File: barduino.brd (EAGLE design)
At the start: 54.9 x 47.4 mm, 25 parts, among them Q2 16MHz, X1 MINI-USB-PWR

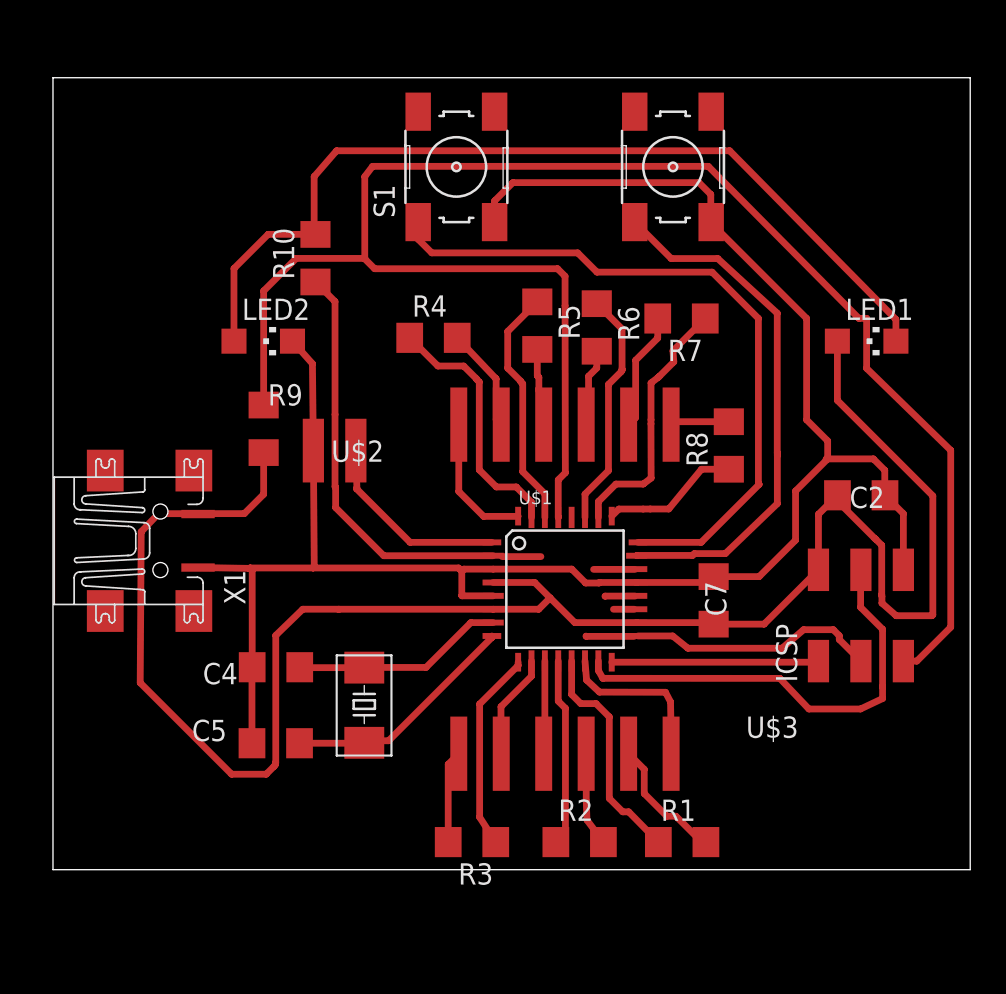
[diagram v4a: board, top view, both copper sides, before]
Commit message: update sch to correctly light AM/PM LEDs
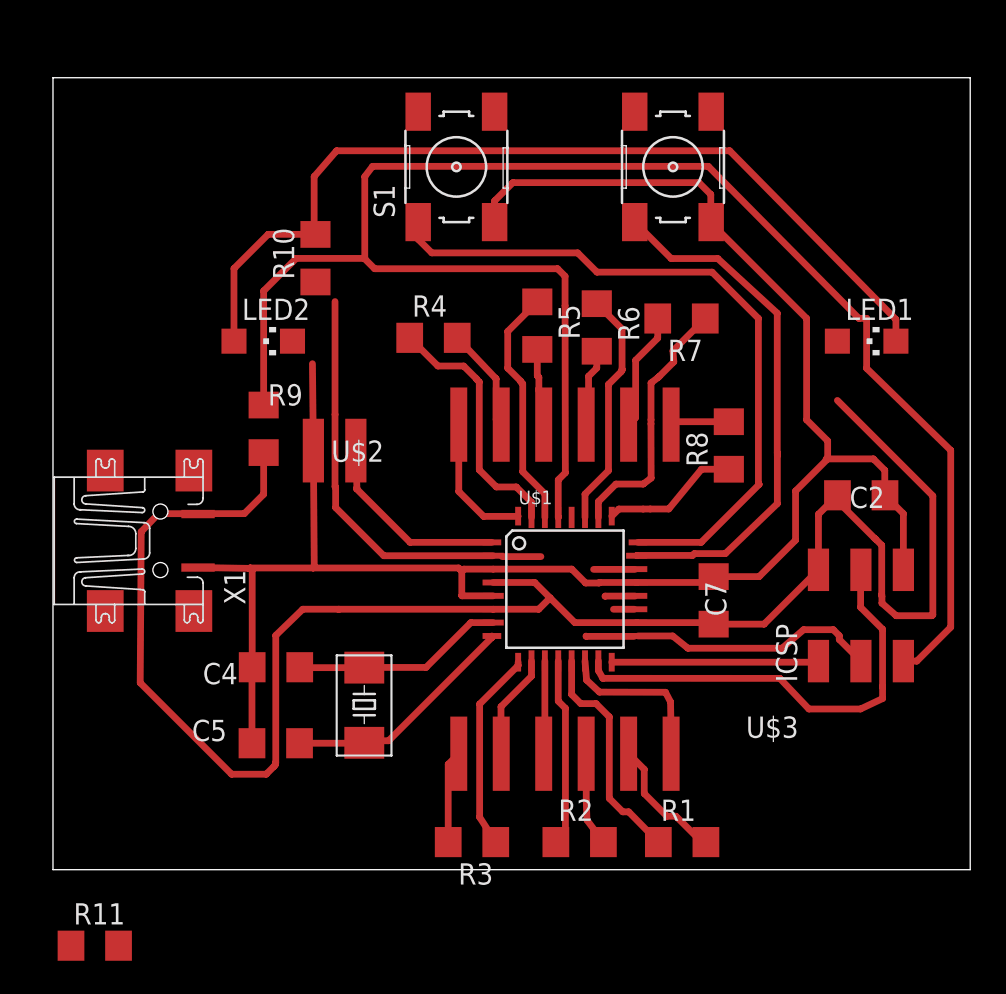
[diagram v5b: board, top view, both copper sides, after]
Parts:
- added R11: (no value), resistor:R1206
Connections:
- removed net N$5: LED1.C, LED2.A, R10.2
- new net N$1: LED1.A, R10.1
- new net N$2: LED2.C, R11.1
- net D4: now also LED1.C, LED2.A; no longer R10.1
- net GND: now also R11.2; no longer LED2.C
- net VCC: now also R10.2; no longer LED1.A
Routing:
- net N$5: track 54.7 -> 0.00 mm
- net D4: track 24.6 -> 77.5 mm
- net VCC: track 111.8 -> 108.2 mm
- net GND: track 115.1 -> 113.3 mm
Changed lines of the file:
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@@
 <element name="R8" library="resistor" package="R1206" value="" x="20.614640625" y="37.693603125" rot="R90"/>
 <element name="X1" library="4-Digit-Clock" package="UX60-MB-5ST-PWR" value="MINI-USB-PWR" x="-13.3858" y="31.991296875"/>
+<element name="R11" library="resistor" package="R1206" value="" x="-17.312640625" y="7.7724"/>
 </elements>
 <signals>
@@
 <wire x1="-4.87171875" y1="27.899359375" x2="-2.748278125" y2="27.899359375" width="0.4064" layer="1"/>
 <wire x1="-2.748278125" y1="27.899359375" x2="-2.698959375" y2="27.8983" width="0.4064" layer="1"/>
-<contactref element="LED1" pad="A"/>
-<wire x1="27.107053125" y1="43.9318375" x2="27.107053125" y2="40.388365625" width="0.4064" layer="1"/>
 <wire x1="27.107053125" y1="40.388365625" x2="32.8168" y2="34.67861875" width="0.4064" layer="1"/>
 <wire x1="32.8168" y1="34.67861875" x2="32.8168" y2="27.56408125" width="0.4064" layer="1"/>
@@
 <wire x1="-11.110196875" y1="33.6169" x2="-11.1358" y2="33.591296875" width="0.4064" layer="1"/>
 <wire x1="-7.21111875" y1="37.26726875" x2="-7.21111875" y2="34.772540625" width="0.4064" layer="1"/>
+<contactref element="R10" pad="2"/>
+<wire x1="-7.21111875" y1="37.26726875" x2="-4.1122625" y2="50.317003125" width="0" layer="19" extent="1-1"/>
 </signal>
 <signal name="GND" class="1">
@@
 <wire x1="-4.183378125" y1="30.406540625" x2="-4.254496875" y2="30.3659" width="0.4064" layer="1"/>
 <wire x1="-4.254496875" y1="30.3659" x2="4.452421875" y2="30.3659" width="0.4064" layer="1"/>
-<contactref element="LED2" pad="C"/>
 <wire x1="-4.23671875" y1="37.3862625" x2="-4.292596875" y2="42.585584375" width="0.4064" layer="1"/>
-<wire x1="-4.292596875" y1="42.585584375" x2="-5.486453125" y2="43.9318375" width="0.4064" layer="1"/>
 <wire x1="19.705265625" y1="29.849740625" x2="22.425321875" y2="29.849740625" width="0.4064" layer="1"/>
 <wire x1="22.425321875" y1="29.849740625" x2="24.60498125" y2="32.0294" width="0.4064" layer="1"/>
@@
 <wire x1="-11.1358" y1="30.391296875" x2="-8.0924375" y2="30.3430375" width="0.4064" layer="1"/>
 <wire x1="-8.0924375" y1="30.3430375" x2="-8.016240625" y2="30.3659" width="0.4064" layer="1"/>
+<contactref element="R11" pad="2"/>
+<wire x1="-15.890640625" y1="7.7724" x2="-7.9091" y2="19.883175" width="0" layer="19" extent="1-1"/>
 </signal>
 <signal name="PB7">
@@
 <wire x1="-2.94131875" y1="35.22875625" x2="-2.941315625" y2="39.54376875" width="0.4064" layer="1"/>
 <wire x1="-2.941315625" y1="46.30205625" x2="-2.941315625" y2="39.54376875" width="0.4064" layer="1"/>
-<contactref element="R10" pad="1"/>
-<wire x1="-4.1122625" y1="47.473003125" x2="-2.941315625" y2="46.30205625" width="0.4064" layer="1"/>
+<contactref element="LED2" pad="A"/>
+<contactref element="LED1" pad="C"/>
+<wire x1="-8.986453125" y1="43.9318375" x2="-8.986453125" y2="48.277846875" width="0.4064" layer="1"/>
+<wire x1="-8.986453125" y1="48.277846875" x2="-6.94181875" y2="50.32248125" width="0.4064" layer="1"/>
+<wire x1="-6.94181875" y1="50.32248125" x2="-4.117740625" y2="50.32248125" width="0.4064" layer="1"/>
+<wire x1="30.56128125" y1="43.977609375" x2="30.607053125" y2="43.9318375" width="0.4064" layer="1"/>
+<wire x1="-4.191" y1="53.774340625" x2="-4.191" y2="50.395740625" width="0.4064" layer="1"/>
+<wire x1="30.607053125" y1="43.9318375" x2="30.607053125" y2="45.23480625" width="0.4064" layer="1"/>
+<wire x1="30.607053125" y1="45.23480625" x2="20.6654375" y2="55.3212" width="0.4064" layer="1"/>
+<wire x1="20.6654375" y1="55.3212" x2="-2.84988125" y2="55.3212" width="0.4064" layer="1"/>
+<wire x1="-2.84988125" y1="55.3212" x2="-4.191" y2="53.774340625" width="0.4064" layer="1"/>
+<wire x1="-4.117740625" y1="50.32248125" x2="-4.191" y2="50.395740625" width="0" layer="19" extent="1-1"/>
+<wire x1="-2.941315625" y1="46.30205625" x2="-4.117740625" y2="50.32248125" width="0" layer="19" extent="1-1"/>
 </signal>
 <signal name="D5">
@@
 <wire x1="12.0852" y1="26.2738" x2="12.0675" y2="26.2915" width="0.4064" layer="1"/>
 </signal>
-<signal name="N$5">
-<contactref element="LED2" pad="A"/>
-<contactref element="LED1" pad="C"/>
-<contactref element="R10" pad="2"/>
-<wire x1="-8.986453125" y1="43.9318375" x2="-8.986453125" y2="48.277846875" width="0.4064" layer="1"/>
-<wire x1="-8.986453125" y1="48.277846875" x2="-6.94181875" y2="50.32248125" width="0.4064" layer="1"/>
-<wire x1="-6.94181875" y1="50.32248125" x2="-4.117740625" y2="50.32248125" width="0.4064" layer="1"/>
-<wire x1="-4.1122625" y1="50.317003125" x2="-4.117740625" y2="50.32248125" width="0.4064" layer="1"/>
-<wire x1="30.56128125" y1="43.977609375" x2="30.607053125" y2="43.9318375" width="0.4064" layer="1"/>
-<wire x1="-4.191" y1="53.774340625" x2="-4.191" y2="50.395740625" width="0.4064" layer="1"/>
-<wire x1="-4.191" y1="50.395740625" x2="-4.1122625" y2="50.317003125" width="0.4064" layer="1"/>
-<wire x1="30.607053125" y1="43.9318375" x2="30.607053125" y2="45.23480625" width="0.4064" layer="1"/>
-<wire x1="30.607053125" y1="45.23480625" x2="20.6654375" y2="55.3212" width="0.4064" layer="1"/>
-<wire x1="20.6654375" y1="55.3212" x2="-2.84988125" y2="55.3212" width="0.4064" layer="1"/>
-<wire x1="-2.84988125" y1="55.3212" x2="-4.191" y2="53.774340625" width="0.4064" layer="1"/>
-</signal>
 <signal name="N$8">
 <contactref element="U$2" pad="6"/>
@@
 <wire x1="15.554959375" y1="18.321140625" x2="14.6203" y2="19.2558" width="0.4064" layer="1"/>
 </signal>
+<signal name="N$1" class="1">
+<contactref element="LED1" pad="A"/>
+<contactref element="R10" pad="1"/>
+<wire x1="-4.1122625" y1="47.473003125" x2="27.107053125" y2="43.9318375" width="0" layer="19" extent="1-1"/>
+</signal>
+<signal name="N$2">
+<contactref element="LED2" pad="C"/>
+<contactref element="R11" pad="1"/>
+<wire x1="-18.734640625" y1="7.7724" x2="-5.486453125" y2="43.9318375" width="0" layer="19" extent="1-1"/>
+</signal>
 </signals>

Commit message: start new AM/PM LED layout
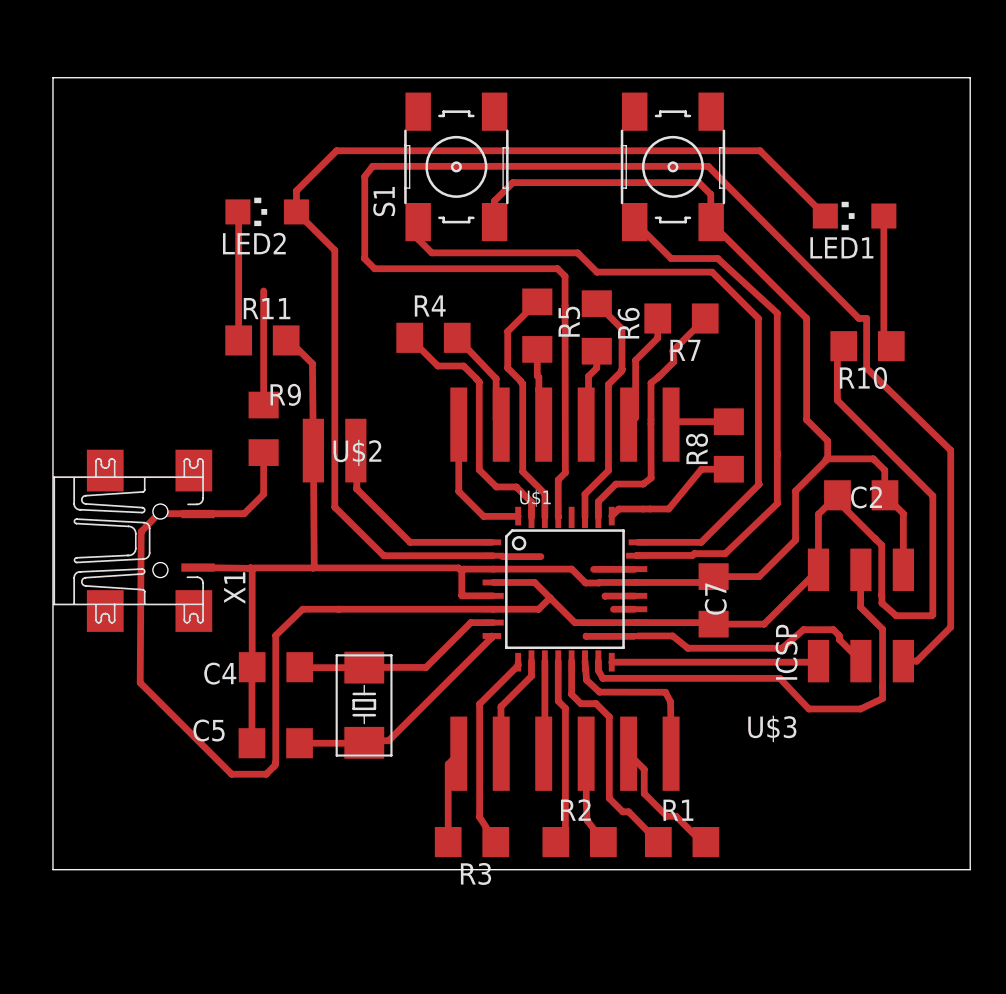
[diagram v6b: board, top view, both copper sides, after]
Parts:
- moved R11 37.6 mm to (-7.28, 44.0)
- moved R10 33.4 mm to (28.9, 43.6), turned to 180 degrees
- moved LED2 7.74 mm to (-7.00, 51.7), turned to 90 degrees
- moved LED1 7.52 mm to (28.1, 51.4), turned to 90 degrees
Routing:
- net D4: track 77.5 -> 64.8 mm
- net N$1: track 0.00 -> 7.97 mm
- net N$2: track 0.00 -> 7.71 mm
- net RESET: track 104.0 -> 97.2 mm
- net VCC: track 108.2 -> 111.6 mm
- net GND: track 113.3 -> 115.5 mm
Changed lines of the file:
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@@
 <element name="R3" library="resistor" package="R1206" value="" x="5.25018125" y="13.97" rot="R180"/>
 <element name="R4" library="resistor" package="R1206" value="" x="2.9464" y="44.132503125"/>
-<element name="LED1" library="led" package="CHIPLED_1206" value="AM" x="28.857053125" y="43.9318375" rot="R270"/>
-<element name="LED2" library="led" package="CHIPLED_1206" value="PM" x="-7.236453125" y="43.9318375" rot="R270"/>
-<element name="R10" library="resistor" package="R1206" value="" x="-4.1122625" y="48.895003125" rot="R90"/>
+<element name="LED1" library="led" package="CHIPLED_1206" value="AM" x="28.135465625" y="51.417225" rot="R90"/>
+<element name="LED2" library="led" package="CHIPLED_1206" value="PM" x="-7.000246875" y="51.663603125" rot="R90"/>
+<element name="R10" library="resistor" package="R1206" value="" x="28.910275" y="43.63211875" rot="R180"/>
 <element name="R5" library="resistor" package="R1206" value="" x="9.156703125" y="44.861478125" rot="R270"/>
 <element name="R6" library="resistor" package="R1206" value="" x="12.715240625" y="44.7522625" rot="R270"/>
@@
 <element name="R8" library="resistor" package="R1206" value="" x="20.614640625" y="37.693603125" rot="R90"/>
 <element name="X1" library="4-Digit-Clock" package="UX60-MB-5ST-PWR" value="MINI-USB-PWR" x="-13.3858" y="31.991296875"/>
-<element name="R11" library="resistor" package="R1206" value="" x="-17.312640625" y="7.7724"/>
+<element name="R11" library="resistor" package="R1206" value="" x="-7.28471875" y="43.975021875"/>
 </elements>
 <signals>
@@
 <wire x1="-4.87171875" y1="27.899359375" x2="-2.748278125" y2="27.899359375" width="0.4064" layer="1"/>
 <wire x1="-2.748278125" y1="27.899359375" x2="-2.698959375" y2="27.8983" width="0.4064" layer="1"/>
-<wire x1="27.107053125" y1="40.388365625" x2="32.8168" y2="34.67861875" width="0.4064" layer="1"/>
+<wire x1="32.8168" y1="34.67861875" x2="27.107053125" y2="40.388365625" width="0.4064" layer="1"/>
 <wire x1="32.8168" y1="34.67861875" x2="32.8168" y2="27.56408125" width="0.4064" layer="1"/>
 <wire x1="32.8168" y1="27.56408125" x2="32.763459375" y2="27.510740625" width="0.4064" layer="1"/>
@@
 <wire x1="-7.21111875" y1="37.26726875" x2="-7.21111875" y2="34.772540625" width="0.4064" layer="1"/>
 <contactref element="R10" pad="2"/>
-<wire x1="-7.21111875" y1="37.26726875" x2="-4.1122625" y2="50.317003125" width="0" layer="19" extent="1-1"/>
+<wire x1="27.107053125" y1="40.388365625" x2="27.107053125" y2="43.250896875" width="0.4064" layer="1"/>
+<wire x1="27.107053125" y1="43.250896875" x2="27.488275" y2="43.63211875" width="0.4064" layer="1"/>
 </signal>
 <signal name="GND" class="1">
@@
 <wire x1="-4.183378125" y1="30.406540625" x2="-4.254496875" y2="30.3659" width="0.4064" layer="1"/>
 <wire x1="-4.254496875" y1="30.3659" x2="4.452421875" y2="30.3659" width="0.4064" layer="1"/>
-<wire x1="-4.23671875" y1="37.3862625" x2="-4.292596875" y2="42.585584375" width="0.4064" layer="1"/>
+<wire x1="-4.292596875" y1="42.585584375" x2="-4.23671875" y2="37.3862625" width="0.4064" layer="1"/>
 <wire x1="19.705265625" y1="29.849740625" x2="22.425321875" y2="29.849740625" width="0.4064" layer="1"/>
 <wire x1="22.425321875" y1="29.849740625" x2="24.60498125" y2="32.0294" width="0.4064" layer="1"/>
@@
 <wire x1="-8.0924375" y1="30.3430375" x2="-8.016240625" y2="30.3659" width="0.4064" layer="1"/>
 <contactref element="R11" pad="2"/>
-<wire x1="-15.890640625" y1="7.7724" x2="-7.9091" y2="19.883175" width="0" layer="19" extent="1-1"/>
+<wire x1="-5.86271875" y1="43.975021875" x2="-5.682034375" y2="43.975021875" width="0.4064" layer="1"/>
+<wire x1="-5.682034375" y1="43.975021875" x2="-4.292596875" y2="42.585584375" width="0.4064" layer="1"/>
 </signal>
 <signal name="PB7">
@@
 <wire x1="28.854403125" y1="42.30878125" x2="28.854403125" y2="45.29581875" width="0.4064" layer="1"/>
 <wire x1="-7.21111875" y1="40.11126875" x2="-7.21111875" y2="46.937753125" width="0.4064" layer="1"/>
-<wire x1="-7.21111875" y1="46.937753125" x2="-5.26626875" y2="48.882603125" width="0.4064" layer="1"/>
-<wire x1="-1.18871875" y1="48.882603125" x2="-5.26626875" y2="48.882603125" width="0.4064" layer="1"/>
 <wire x1="10.817859375" y1="46.05390625" x2="10.817859375" y2="47.818040625" width="0.4064" layer="1"/>
 <wire x1="10.817859375" y1="47.818040625" x2="10.37081875" y2="48.26508125" width="0.4064" layer="1"/>
@@
 <wire x1="-1.16331875" y1="53.77688125" x2="-1.16331875" y2="48.908003125" width="0.4064" layer="1"/>
 <wire x1="-1.16331875" y1="48.908003125" x2="-1.18871875" y2="48.882603125" width="0.4064" layer="1"/>
+<wire x1="-7.21111875" y1="46.937753125" x2="-1.18871875" y2="48.882603125" width="0" layer="19" extent="1-1"/>
 </signal>
 <signal name="PB6">
@@
 <contactref element="U$1" pad="2"/>
 <wire x1="6.5177" y1="31.0983" x2="-0.026478125" y2="31.0983" width="0.4064" layer="1"/>
-<wire x1="-0.026478125" y1="31.0983" x2="-2.905759375" y2="33.97758125" width="0.4064" layer="1"/>
-<wire x1="-2.905759375" y1="33.97758125" x2="-2.905759375" y2="35.193196875" width="0.4064" layer="1"/>
-<wire x1="-2.905759375" y1="35.193196875" x2="-2.94131875" y2="35.22875625" width="0.4064" layer="1"/>
-<wire x1="-2.94131875" y1="35.22875625" x2="-2.941315625" y2="39.54376875" width="0.4064" layer="1"/>
-<wire x1="-2.941315625" y1="46.30205625" x2="-2.941315625" y2="39.54376875" width="0.4064" layer="1"/>
+<wire x1="-0.026478125" y1="31.0983" x2="-2.95401875" y2="34.000440625" width="0.4064" layer="1"/>
 <contactref element="LED2" pad="A"/>
 <contactref element="LED1" pad="C"/>
-<wire x1="-8.986453125" y1="43.9318375" x2="-8.986453125" y2="48.277846875" width="0.4064" layer="1"/>
-<wire x1="-8.986453125" y1="48.277846875" x2="-6.94181875" y2="50.32248125" width="0.4064" layer="1"/>
-<wire x1="-6.94181875" y1="50.32248125" x2="-4.117740625" y2="50.32248125" width="0.4064" layer="1"/>
-<wire x1="30.56128125" y1="43.977609375" x2="30.607053125" y2="43.9318375" width="0.4064" layer="1"/>
-<wire x1="-4.191" y1="53.774340625" x2="-4.191" y2="50.395740625" width="0.4064" layer="1"/>
-<wire x1="30.607053125" y1="43.9318375" x2="30.607053125" y2="45.23480625" width="0.4064" layer="1"/>
-<wire x1="30.607053125" y1="45.23480625" x2="20.6654375" y2="55.3212" width="0.4064" layer="1"/>
-<wire x1="20.6654375" y1="55.3212" x2="-2.84988125" y2="55.3212" width="0.4064" layer="1"/>
-<wire x1="-2.84988125" y1="55.3212" x2="-4.191" y2="53.774340625" width="0.4064" layer="1"/>
-<wire x1="-4.117740625" y1="50.32248125" x2="-4.191" y2="50.395740625" width="0" layer="19" extent="1-1"/>
-<wire x1="-2.941315625" y1="46.30205625" x2="-4.117740625" y2="50.32248125" width="0" layer="19" extent="1-1"/>
+<wire x1="-5.250246875" y1="51.663603125" x2="-5.250246875" y2="52.920834375" width="0.4064" layer="1"/>
+<wire x1="-5.250246875" y1="52.920834375" x2="-2.84988125" y2="55.3212" width="0.4064" layer="1"/>
+<wire x1="22.481490625" y1="55.3212" x2="26.385465625" y2="51.417225" width="0.4064" layer="1"/>
+<wire x1="-2.84988125" y1="55.3212" x2="22.481490625" y2="55.3212" width="0.4064" layer="1"/>
+<wire x1="-2.95401875" y1="34.000440625" x2="-2.95401875" y2="49.367375" width="0.4064" layer="1"/>
+<wire x1="-2.95401875" y1="49.367375" x2="-5.250246875" y2="51.663603125" width="0.4064" layer="1"/>
 </signal>
 <signal name="D5">
@@
 <contactref element="LED1" pad="A"/>
 <contactref element="R10" pad="1"/>
-<wire x1="-4.1122625" y1="47.473003125" x2="27.107053125" y2="43.9318375" width="0" layer="19" extent="1-1"/>
+<wire x1="29.885465625" y1="51.417225" x2="29.885465625" y2="44.078928125" width="0.4064" layer="1"/>
+<wire x1="29.885465625" y1="44.078928125" x2="30.332275" y2="43.63211875" width="0.4064" layer="1"/>
 </signal>
 <signal name="N$2">
 <contactref element="LED2" pad="C"/>
 <contactref element="R11" pad="1"/>
-<wire x1="-18.734640625" y1="7.7724" x2="-5.486453125" y2="43.9318375" width="0" layer="19" extent="1-1"/>
+<wire x1="-8.70671875" y1="43.975021875" x2="-8.70671875" y2="51.620075" width="0.4064" layer="1"/>
+<wire x1="-8.70671875" y1="51.620075" x2="-8.750246875" y2="51.663603125" width="0.4064" layer="1"/>
 </signal>
 </signals>
